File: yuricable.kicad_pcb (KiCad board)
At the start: 2 copper layers, 66 x 25.4 mm, 14 parts, among them U1 FlipperZero

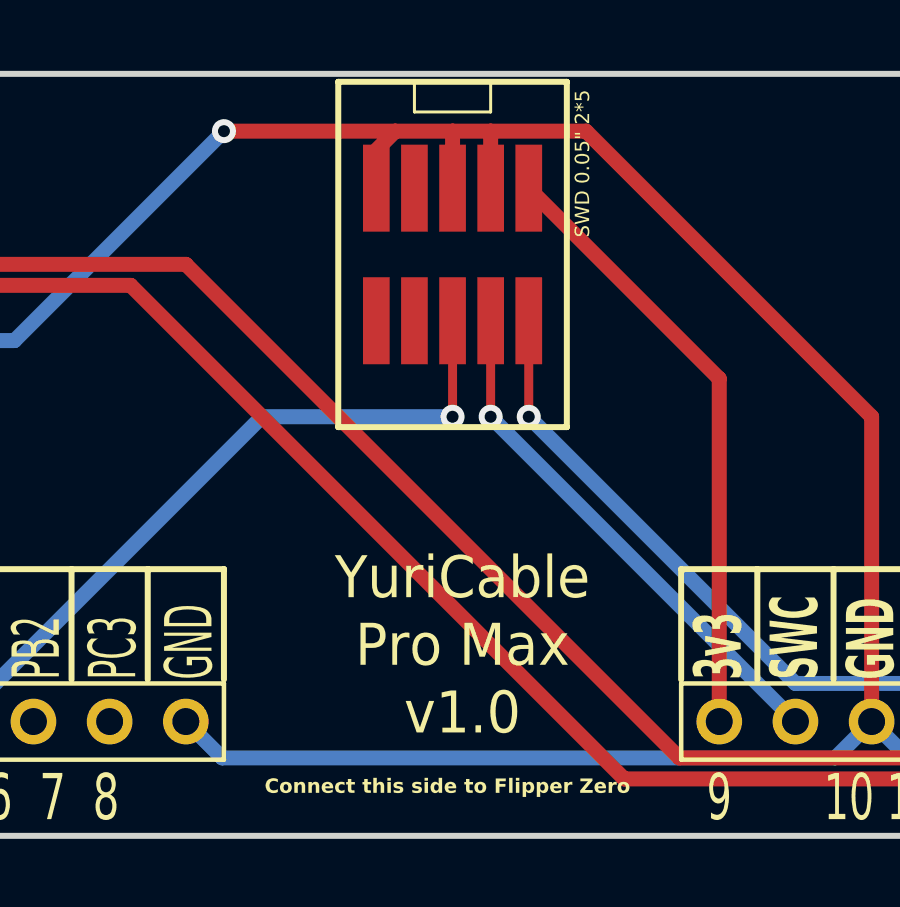
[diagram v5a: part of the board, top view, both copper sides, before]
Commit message: fixed smd pads to be masked (aka solderable)
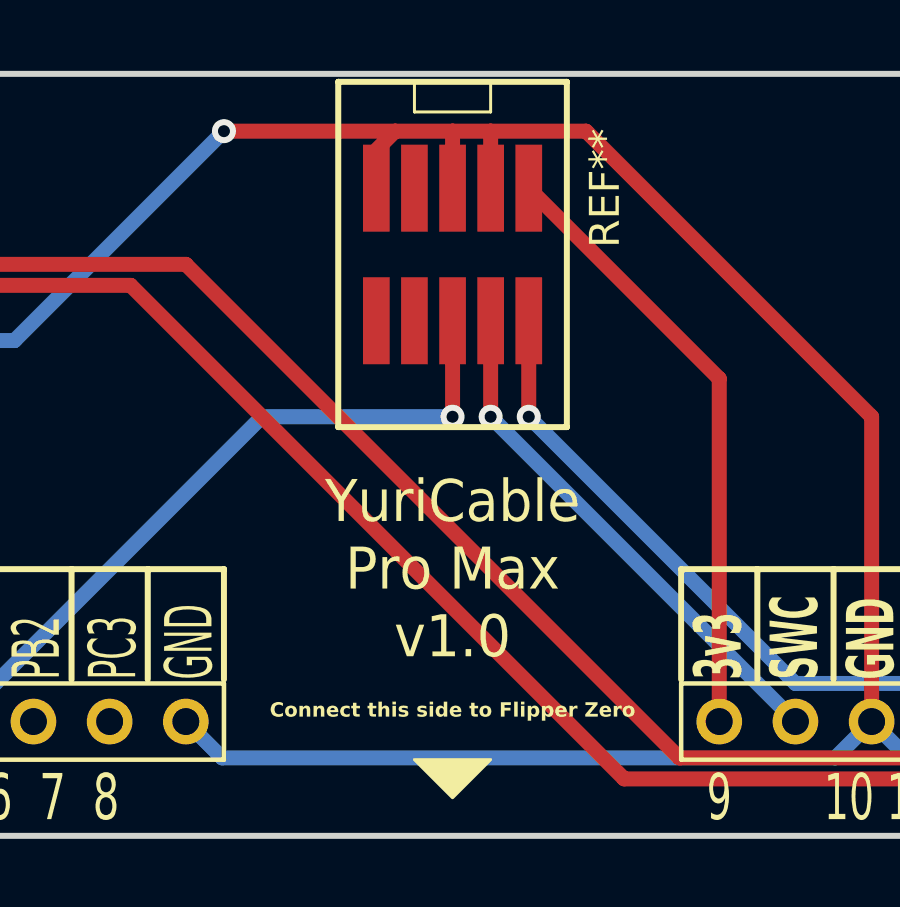
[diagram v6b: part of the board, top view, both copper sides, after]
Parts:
- removed SWD 0.05" 2*5: SWD_0.05_2x5, ARM-JTAG-SWD:SWD_0.05_2x5
- added REF**: SWD_0.05_2x5, ARM-JTAG-SWD:SWD_0.05_2x5, F.Cu at (90.2, 61.0)
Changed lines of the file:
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@@
   (net 15 "/PA6")
   (net 16 "/PA7")
-  (net 17 "/RXI")
-  (net 18 "TXO")
-  (net 19 "RESET")
   (footprint "lomalkin_kicad_footprints:FlipperZero" locked (layer "F.Cu")
     (at 90.17 76.2)
@@
       (net 15 "/PA6"))
   )
-  (footprint "" (layer "F.Cu")
-    (at 63.5 60.96)
-    (fp_text reference "" (at 0 0) (layer "F.SilkS")
-        (effects (font (size 1.27 1.27) (thickness 0.15)))
-    )
-    (fp_text value "" (at 0 0) (layer "F.SilkS")
-        (effects (font (size 1.27 1.27) (thickness 0.15)))
-    )
-    (pad "8" thru_hole circle (at 0 0 270) (size 1.524 1.524) (drill 0.9) (layers "*.Cu" "*.Mask")
-      (net 3 "GND"))
-  )
-  (footprint "" (layer "F.Cu")
-    (at 63.5 60.96)
-    (fp_text reference "" (at 0 0) (layer "F.SilkS")
-        (effects (font (size 1.27 1.27) (thickness 0.15)))
-    )
-    (fp_text value "" (at 0 0) (layer "F.SilkS")
-        (effects (font (size 1.27 1.27) (thickness 0.15)))
-    )
-    (pad "8" thru_hole circle (at 0 0 270) (size 1.524 1.524) (drill 0.9) (layers "*.Cu" "*.Mask")
-      (net 3 "GND"))
-  )
-  (footprint "" (layer "F.Cu")
-    (at 68.58 58.42)
-    (fp_text reference "" (at 0 0) (layer "F.SilkS")
-        (effects (font (size 1.27 1.27) (thickness 0.15)))
-    )
-    (fp_text value "" (at 0 0) (layer "F.SilkS")
-        (effects (font (size 1.27 1.27) (thickness 0.15)))
-    )
-    (pad "14" thru_hole circle (at 0 0 270) (size 1.524 1.524) (drill 0.9) (layers "*.Cu" "*.Mask")
-      (net 7 "/UART_RX"))
-  )
-  (footprint "" (layer "F.Cu")
-    (at 66.04 58.42)
-    (fp_text reference "" (at 0 0) (layer "F.SilkS")
-        (effects (font (size 1.27 1.27) (thickness 0.15)))
-    )
-    (fp_text value "" (at 0 0) (layer "F.SilkS")
-        (effects (font (size 1.27 1.27) (thickness 0.15)))
-    )
-    (pad "3" thru_hole circle (at 0 0 270) (size 1.524 1.524) (drill 0.9) (layers "*.Cu" "*.Mask")
-      (net 15 "/PA6"))
-  )
   (footprint "ARM-JTAG-SWD:SWD_0.05_2x5" (layer "F.Cu")
     (at 90.17 60.96)
     (attr smd)
-    (fp_text reference "SWD 0.05\" 2*5" (at 4.33 -3.36 90 unlocked) (layer "F.SilkS")
-        (effects (font (size 0.48 0.48) (thickness 0.12)))
+    (fp_text reference "REF**" (at 5.08 -2.54 90 unlocked) (layer "F.SilkS")
+        (effects (font (size 1 1) (thickness 0.1)))
     )
     (fp_text value "SWD_0.05_2x5" (at 6.35 0 90 unlocked) (layer "F.Fab")
@@
     (fp_line (start 3.81 5.425) (end 3.81 -6.085)
       (stroke (width 0.2) (type default)) (layer "F.SilkS"))
-    (pad "GND1" smd rect (at 1.27 -2.54) (size 0.89 2.9) (layers "F.Cu")
-      (net 3 "GND") (thermal_bridge_angle 45))
-    (pad "GND2" smd rect (at 0 -2.54) (size 0.89 2.9) (layers "F.Cu")
-      (net 3 "GND") (thermal_bridge_angle 45))
-    (pad "GND3" smd rect (at -2.54 -2.54) (size 0.89 2.9) (layers "F.Cu")
-      (net 3 "GND") (thermal_bridge_angle 45))
-    (pad "RESET" smd rect (at -2.54 1.88) (size 0.89 2.9) (layers "F.Cu")
-      (net 19 "RESET") (thermal_bridge_angle 45))
-    (pad "RXI" smd rect (at -1.27 -2.54) (size 0.89 2.9) (layers "F.Cu")
-      (net 17 "/RXI") (thermal_bridge_angle 45))
-    (pad "SWCLK" smd rect (at 1.27 1.88) (size 0.89 2.9) (layers "F.Cu")
-      (net 10 "/SWCLK") (thermal_bridge_angle 45))
-    (pad "SWDIO" smd rect (at 2.54 1.88) (size 0.89 2.9) (layers "F.Cu")
-      (net 9 "/SWDIO") (thermal_bridge_angle 45))
-    (pad "SWO" smd rect (at 0 1.88) (size 0.89 2.9) (layers "F.Cu")
-      (net 13 "/SWO") (thermal_bridge_angle 45))
-    (pad "TXO" smd rect (at -1.27 1.88) (size 0.89 2.9) (layers "F.Cu")
-      (net 18 "TXO") (thermal_bridge_angle 45))
-    (pad "VREF" smd rect (at 2.54 -2.54) (size 0.89 2.9) (layers "F.Cu")
-      (net 2 "/3.3V") (thermal_bridge_angle 45))
+    (pad "GND1" smd rect (at 1.27 -2.54) (size 0.89 2.9) (layers "F.Cu" "F.Mask")
+      (thermal_bridge_angle 45))
+    (pad "GND2" smd rect (at 0 -2.54) (size 0.89 2.9) (layers "F.Cu" "F.Mask")
+      (thermal_bridge_angle 45))
+    (pad "GND3" smd rect (at -2.54 -2.54) (size 0.89 2.9) (layers "F.Cu" "F.Mask")
+      (thermal_bridge_angle 45))
+    (pad "RESET" smd rect (at -2.54 1.88) (size 0.89 2.9) (layers "F.Cu" "F.Mask")
+      (thermal_bridge_angle 45))
+    (pad "RXI" smd rect (at -1.27 -2.54) (size 0.89 2.9) (layers "F.Cu" "F.Mask")
+      (thermal_bridge_angle 45))
+    (pad "SWCLK" smd rect (at 1.27 1.88) (size 0.89 2.9) (layers "F.Cu" "F.Mask")
+      (thermal_bridge_angle 45))
+    (pad "SWDIO" smd rect (at 2.54 1.88) (size 0.89 2.9) (layers "F.Cu" "F.Mask")
+      (thermal_bridge_angle 45))
+    (pad "SWO" smd rect (at 0 1.88) (size 0.89 2.9) (layers "F.Cu" "F.Mask")
+      (thermal_bridge_angle 45))
+    (pad "TXO" smd rect (at -1.27 1.88) (size 0.89 2.9) (layers "F.Cu" "F.Mask")
+      (thermal_bridge_angle 45))
+    (pad "VREF" smd rect (at 2.54 -2.54) (size 0.89 2.9) (layers "F.Cu" "F.Mask")
+      (thermal_bridge_angle 45))
+  )
+  (footprint "" (layer "F.Cu")
+    (at 63.5 60.96)
+    (fp_text reference "" (at 0 0) (layer "F.SilkS")
+        (effects (font (size 1.27 1.27) (thickness 0.15)))
+    )
+    (fp_text value "" (at 0 0) (layer "F.SilkS")
+        (effects (font (size 1.27 1.27) (thickness 0.15)))
+    )
+    (pad "8" thru_hole circle (at 0 0 270) (size 1.524 1.524) (drill 0.9) (layers "*.Cu" "*.Mask")
+      (net 3 "GND"))
+  )
+  (footprint "" (layer "F.Cu")
+    (at 63.5 60.96)
+    (fp_text reference "" (at 0 0) (layer "F.SilkS")
+        (effects (font (size 1.27 1.27) (thickness 0.15)))
+    )
+    (fp_text value "" (at 0 0) (layer "F.SilkS")
+        (effects (font (size 1.27 1.27) (thickness 0.15)))
+    )
+    (pad "8" thru_hole circle (at 0 0 270) (size 1.524 1.524) (drill 0.9) (layers "*.Cu" "*.Mask")
+      (net 3 "GND"))
+  )
+  (footprint "" (layer "F.Cu")
+    (at 68.58 58.42)
+    (fp_text reference "" (at 0 0) (layer "F.SilkS")
+        (effects (font (size 1.27 1.27) (thickness 0.15)))
+    )
+    (fp_text value "" (at 0 0) (layer "F.SilkS")
+        (effects (font (size 1.27 1.27) (thickness 0.15)))
+    )
+    (pad "14" thru_hole circle (at 0 0 270) (size 1.524 1.524) (drill 0.9) (layers "*.Cu" "*.Mask")
+      (net 7 "/UART_RX"))
   )
   (footprint "" (layer "F.Cu")
@@
   )
   (footprint "" (layer "F.Cu")
+    (at 66.04 58.42)
+    (fp_text reference "" (at 0 0) (layer "F.SilkS")
+        (effects (font (size 1.27 1.27) (thickness 0.15)))
+    )
+    (fp_text value "" (at 0 0) (layer "F.SilkS")
+        (effects (font (size 1.27 1.27) (thickness 0.15)))
+    )
+    (pad "3" thru_hole circle (at 0 0 270) (size 1.524 1.524) (drill 0.9) (layers "*.Cu" "*.Mask")
+      (net 15 "/PA6"))
+  )
+  (footprint "" (layer "F.Cu")
     (at 63.5 58.42)
     (fp_text reference "" (at 0 0) (layer "F.SilkS")
@@
   (gr_line (start 118.11 71.12) (end 118.11 74.8)
     (stroke (width 0.2) (type solid)) (layer "F.SilkS"))
+  (gr_poly
+    (pts
+      (xy 88.9 77.47)
+      (xy 90.17 78.74)
+      (xy 91.44 77.47)
+    )
+    (stroke (width 0.1) (type solid)) (fill solid) (layer "F.SilkS"))
   (gr_line (start 62.23 59.7) (end 67.31 59.7)
     (stroke (width 0.2) (type solid)) (layer "F.SilkS"))
@@
     )
   )
-  (gr_text "YuriCable \nPro Max \nv1.0" (at 90.5 73.66) (layer "F.SilkS")
+  (gr_text "YuriCable \nPro Max \nv1.0" (at 90.17 71.12) (layer "F.SilkS")
     (effects (font (size 1.4 1.3) (thickness 0.3)))
   )
@@
     (effects (font (size 1.5 0.8) (thickness 0.2) bold) (justify left))
   )
-  (gr_text "Connect this side to Flipper Zero\n\n" (at 90 78.74) (layer "F.SilkS")
+  (gr_text "Connect this side to Flipper Zero\n\n" (at 90.17 76.2) (layer "F.SilkS")
     (effects (font (size 0.48 0.48) (thickness 0.12) bold))
   )
@@
   (segment (start 81.28 60.96) (end 97.732 77.412) (width 0.5) (layer "F.Cu") (net 8))
   (segment (start 97.732 77.412) (end 108.008 77.412) (width 0.5) (layer "F.Cu") (net 8))
-  (segment (start 92.71 62.84) (end 92.71 66.04) (width 0.3) (layer "F.Cu") (net 9))
+  (segment (start 92.71 62.84) (end 92.71 66.04) (width 0.5) (layer "F.Cu") (net 9))
   (via (at 92.71 66.04) (size 0.8) (drill 0.4) (layers "F.Cu" "B.Cu") (net 9))
   (segment (start 101.6 74.93) (end 92.71 66.04) (width 0.5) (layer "B.Cu") (net 9))
   (segment (start 106.68 76.2) (end 105.41 74.93) (width 0.5) (layer "B.Cu") (net 9))
   (segment (start 105.41 74.93) (end 101.6 74.93) (width 0.5) (layer "B.Cu") (net 9))
-  (segment (start 91.44 62.84) (end 91.44 66.04) (width 0.3) (layer "F.Cu") (net 10))
+  (segment (start 91.44 62.84) (end 91.44 66.04) (width 0.5) (layer "F.Cu") (net 10))
   (via (at 91.44 66.04) (size 0.8) (drill 0.4) (layers "F.Cu" "B.Cu") (net 10))
   (segment (start 101.6 76.2) (end 91.44 66.04) (width 0.5) (layer "B.Cu") (net 10))
-  (segment (start 90.17 62.84) (end 90.17 66.04) (width 0.3) (layer "F.Cu") (net 13))
+  (segment (start 90.17 62.84) (end 90.17 66.04) (width 0.5) (layer "F.Cu") (net 13))
   (via (at 90.17 66.04) (size 0.8) (drill 0.4) (layers "F.Cu" "B.Cu") (net 13))
   (segment (start 73.66 76.2) (end 83.82 66.04) (width 0.5) (layer "B.Cu") (net 13))

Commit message: removed that one small trace
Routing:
- net GND: track 107.2 -> 106.0 mm
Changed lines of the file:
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@@
   (segment (start 99.06 64.77) (end 92.71 58.42) (width 0.5) (layer "F.Cu") (net 2))
   (segment (start 99.06 76.2) (end 99.06 64.77) (width 0.5) (layer "F.Cu") (net 2))
-  (segment (start 104.14 66.04) (end 104.14 76.2) (width 0.5) (layer "F.Cu") (net 3))
   (segment (start 87.63 57.15) (end 88.26 56.52) (width 0.5) (layer "F.Cu") (net 3))
   (segment (start 91.44 56.52) (end 91.44 58.42) (width 0.5) (layer "F.Cu") (net 3))
@@
   (segment (start 88.26 56.52) (end 82.55 56.52) (width 0.5) (layer "F.Cu") (net 3))
   (segment (start 90.17 56.52) (end 91.44 56.52) (width 0.5) (layer "F.Cu") (net 3))
-  (segment (start 104.14 67.255) (end 104.14 66.04) (width 0.3) (layer "F.Cu") (net 3))
+  (segment (start 94.62 56.52) (end 104.14 66.04) (width 0.5) (layer "F.Cu") (net 3))
+  (segment (start 104.14 66.04) (end 104.14 76.2) (width 0.5) (layer "F.Cu") (net 3))
+  (segment (start 88.26 56.52) (end 90.17 56.52) (width 0.5) (layer "F.Cu") (net 3))
   (segment (start 91.44 56.52) (end 94.62 56.52) (width 0.5) (layer "F.Cu") (net 3))
-  (segment (start 94.62 56.52) (end 104.14 66.04) (width 0.5) (layer "F.Cu") (net 3))
-  (segment (start 88.26 56.52) (end 90.17 56.52) (width 0.5) (layer "F.Cu") (net 3))
   (via (at 82.55 56.52) (size 0.8) (drill 0.4) (layers "F.Cu" "B.Cu") (net 3))
   (segment (start 75.57 63.5) (end 66.04 63.5) (width 0.5) (layer "B.Cu") (net 3))

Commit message: added pads for usb-a cable side
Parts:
- added ?: , , F.Cu at (121.9, 63.5)
- added ?: , , F.Cu at (121.9, 66.0)
- added ?: , ARM-JTAG-SWD:Pad, F.Cu at (76.2, 58.4)
- added ?: , ARM-JTAG-SWD:Pad, F.Cu at (121.9, 61.0)
- added ?: , ARM-JTAG-SWD:Pad, F.Cu at (121.9, 63.5)
- added ?: , ARM-JTAG-SWD:Pad, F.Cu at (121.9, 66.0)
- added ?: , ARM-JTAG-SWD:Pad, F.Cu at (73.7, 58.4)
- added ?: , ARM-JTAG-SWD:Pad, F.Cu at (121.9, 58.4)
- added ?: , , F.Cu at (121.9, 58.4)
- added ?: , , F.Cu at (121.9, 61.0)
- SWD 0.05" 2*5: renamed from REF**
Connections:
- SWD 0.05" 2*5 pad GND1: (no net) -> GND
- SWD 0.05" 2*5 pad GND2: (no net) -> GND
- SWD 0.05" 2*5 pad GND3: (no net) -> GND
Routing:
- net (no net): track 0.00 -> 104.4 mm
- net /5V: track 19.9 -> 86.5 mm, vias 0 -> 1
- net GND: track 106.0 -> 131.4 mm
- net /PA6: track 18.8 -> 17.6 mm
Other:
- board text added: "L1n"
- board text added: "L1p"
